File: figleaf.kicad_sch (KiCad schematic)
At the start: 70 parts, among them J1 Conn_01x02_Pin, J2 HRO_TYPE-C-31-M-14, J3 Battery, J9 TC2030_SWD, Q2 2N7002, SW1 PWR, SW2 RST, U1 SRV05-4, U10 MAX17048, U3 BQ24075, U8 nRF52840_moko_mk08

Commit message: data line thickness + mounting cuts
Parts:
- U8: footprint PCM_marbastlib-various:nRF52840_moko_mk08 -> Graz_Footprints:nRF52840_moko_mk08_GRAZ
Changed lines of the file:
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@@
 			)
 		)
-		(property "Footprint" "PCM_marbastlib-various:nRF52840_moko_mk08"
+		(property "Footprint" "Graz_Footprints:nRF52840_moko_mk08_GRAZ"
 			(at 87.63 118.11 90)
 			(effects

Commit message: testing m2 mounting holes
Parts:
- H1, H2, H3, H4, H5, H6, H7: footprint Graz_Footprints:m1.6 -> Graz_Footprints:MountingHole_M2_Graz
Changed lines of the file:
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@@
 			)
 		)
-		(property "Footprint" "Graz_Footprints:m1.6"
+		(property "Footprint" "Graz_Footprints:MountingHole_M2_Graz"
 			(at 43.18 176.53 0)
 			(effects
@@
 			)
 		)
-		(property "Footprint" "Graz_Footprints:m1.6"
+		(property "Footprint" "Graz_Footprints:MountingHole_M2_Graz"
 			(at 83.82 176.53 0)
 			(effects
@@
 			)
 		)
-		(property "Footprint" "Graz_Footprints:m1.6"
+		(property "Footprint" "Graz_Footprints:MountingHole_M2_Graz"
 			(at 63.5 176.53 0)
 			(effects
@@
 			)
 		)
-		(property "Footprint" "Graz_Footprints:m1.6"
+		(property "Footprint" "Graz_Footprints:MountingHole_M2_Graz"
 			(at 22.86 191.77 0)
 			(effects
@@
 			)
 		)
-		(property "Footprint" "Graz_Footprints:m1.6"
+		(property "Footprint" "Graz_Footprints:MountingHole_M2_Graz"
 			(at 63.5 191.77 0)
 			(effects
@@
 			)
 		)
-		(property "Footprint" "Graz_Footprints:m1.6"
+		(property "Footprint" "Graz_Footprints:MountingHole_M2_Graz"
 			(at 43.18 191.77 0)
 			(effects
@@
 			)
 		)
-		(property "Footprint" "Graz_Footprints:m1.6"
+		(property "Footprint" "Graz_Footprints:MountingHole_M2_Graz"
 			(at 22.86 176.53 0)
 			(effects

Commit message: finish m2 refactor
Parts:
- added H8, H9: MountingHole, Graz_Footprints:MountingHole_M2_Graz, symbol Mechanical:MountingHole
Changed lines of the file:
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@@
 	)
 	(symbol
+		(lib_id "Mechanical:MountingHole")
+		(at 83.82 191.77 0)
+		(unit 1)
+		(exclude_from_sim no)
+		(in_bom no)
+		(on_board yes)
+		(dnp no)
+		(fields_autoplaced yes)
+		(property "Reference" "H8"
+			(at 86.36 190.4999 0)
+			(effects
+				(font
+					(size 1.27 1.27)
+				)
+				(justify left)
+			)
+		)
+		(property "Value" "MountingHole"
+			(at 86.36 193.0399 0)
+			(effects
+				(font
+					(size 1.27 1.27)
+				)
+				(justify left)
+			)
+		)
+		(property "Footprint" "Graz_Footprints:MountingHole_M2_Graz"
+			(at 83.82 191.77 0)
+			(effects
+				(font
+					(size 1.27 1.27)
+				)
+				(hide yes)
+			)
+		)
+		(property "Datasheet" "~"
+			(at 83.82 191.77 0)
+			(effects
+				(font
+					(size 1.27 1.27)
+				)
+				(hide yes)
+			)
+		)
+		(property "Description" "Mounting Hole without connection"
+			(at 83.82 191.77 0)
+			(effects
+				(font
+					(size 1.27 1.27)
+				)
+				(hide yes)
+			)
+		)
+		(instances
+			(project "figleaf"
+				(path "/49b93484-acc8-4f70-93bc-7a6072a35fe8"
+					(reference "H8")
+					(unit 1)
+				)
+			)
+		)
+	)
+	(symbol
 		(lib_id "Device:Polyfuse_Small")
 		(at 64.77 29.21 90)
@@
 					(unit 1)
 				)
+			)
+		)
+	)
+	(symbol
+		(lib_id "Mechanical:MountingHole")
+		(at 104.14 191.77 0)
+		(unit 1)
+		(exclude_from_sim no)
+		(in_bom no)
+		(on_board yes)
+		(dnp no)
+		(fields_autoplaced yes)
+		(property "Reference" "H9"
+			(at 106.68 190.4999 0)
+			(effects
+				(font
+					(size 1.27 1.27)
+				)
+				(justify left)
+			)
+		)
+		(property "Value" "MountingHole"
+			(at 106.68 193.0399 0)
+			(effects
+				(font
+					(size 1.27 1.27)
+				)
+				(justify left)
+			)
+		)
+		(property "Footprint" "Graz_Footprints:MountingHole_M2_Graz"
+			(at 104.14 191.77 0)
+			(effects
+				(font
+					(size 1.27 1.27)
+				)
+				(hide yes)
+			)
+		)
+		(property "Datasheet" "~"
+			(at 104.14 191.77 0)
+			(effects
+				(font
+					(size 1.27 1.27)
+				)
+				(hide yes)
+			)
+		)
+		(property "Description" "Mounting Hole without connection"
+			(at 104.14 191.77 0)
+			(effects
+				(font
+					(size 1.27 1.27)
+				)
+				(hide yes)
+			)
+		)
+		(instances
+			(project "figleaf"
+				(path "/49b93484-acc8-4f70-93bc-7a6072a35fe8"
+					(reference "H9")
+					(unit 1)
+				)

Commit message: pre right side
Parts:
- added TP1, TP2: TestPoint_Probe, TestPoint:TestPoint_Pad_D1.0mm, symbol Connector:TestPoint_Probe
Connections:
- net USB-D+: now also TP2.1
- net USB-D-: now also TP1.1
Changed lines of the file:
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@@
 	)
 	(junction
+		(at 67.31 101.6)
+		(diameter 0)
+		(color 0 0 0 0)
+	)
+	(junction
 		(at 93.98 158.75)
 		(diameter 0)
@@
 	)
 	(junction
+		(at 67.31 104.14)
+		(diameter 0)
+		(color 0 0 0 0)
+	)
+	(junction
 		(at 49.53 29.21)
 		(diameter 0)
@@
 	(wire
 		(pts
+			(xy 67.31 104.14) (xy 69.85 104.14)
+		)
+		(stroke
+			(width 0)
+			(type default)
+		)
+	)
+	(wire
+		(pts
 			(xy 349.25 142.24) (xy 354.33 142.24)
 		)
@@
 	(wire
 		(pts
+			(xy 64.77 99.06) (xy 69.85 99.06)
+		)
+		(stroke
+			(width 0)
+			(type default)
+		)
+	)
+	(wire
+		(pts
 			(xy 49.53 29.21) (xy 55.88 29.21)
 		)
@@
 	(wire
 		(pts
+			(xy 67.31 101.6) (xy 69.85 101.6)
+		)
+		(stroke
+			(width 0)
+			(type default)
+		)
+	)
+	(wire
+		(pts
 			(xy 313.69 127) (xy 313.69 132.08)
 		)
@@
 	(wire
 		(pts
+			(xy 64.77 104.14) (xy 67.31 104.14)
+		)
+		(stroke
+			(width 0)
+			(type default)
+		)
+	)
+	(wire
+		(pts
 			(xy 262.89 152.4) (xy 262.89 157.48)
 		)
@@
 	(wire
 		(pts
+			(xy 64.77 101.6) (xy 67.31 101.6)
+		)
+		(stroke
+			(width 0)
+			(type default)
+		)
+	)
+	(wire
+		(pts
 			(xy 267.97 127) (xy 267.97 132.08)
 		)
@@
 	(global_label "USB-D+"
 		(shape bidirectional)
-		(at 69.85 101.6 180)
+		(at 64.77 101.6 180)
 		(fields_autoplaced yes)
 		(effects
@@
 		)
 		(property "Intersheetrefs" "${INTERSHEET_REFS}"
-			(at 59.2121 101.6794 0)
+			(at 54.1321 101.6794 0)
 			(effects
 				(font
@@
 	(global_label "USB-D-"
 		(shape bidirectional)
-		(at 69.85 104.14 180)
+		(at 64.77 104.14 180)
 		(fields_autoplaced yes)
 		(effects
@@
 		)
 		(property "Intersheetrefs" "${INTERSHEET_REFS}"
-			(at 59.2121 104.2194 0)
+			(at 54.1321 104.2194 0)
 			(effects
 				(font
@@
 	)
 	(symbol
+		(lib_id "Connector:TestPoint_Probe")
+		(at 67.31 101.6 90)
+		(unit 1)
+		(exclude_from_sim no)
+		(in_bom yes)
+		(on_board yes)
+		(dnp no)
+		(fields_autoplaced yes)
+		(property "Reference" "TP2"
+			(at 65.7225 93.98 90)
+			(effects
+				(font
+					(size 1.27 1.27)
+				)
+			)
+		)
+		(property "Value" "TestPoint_Probe"
+			(at 65.7225 96.52 90)
+			(effects
+				(font
+					(size 1.27 1.27)
+				)
+			)
+		)
+		(property "Footprint" "TestPoint:TestPoint_Pad_D1.0mm"
+			(at 67.31 96.52 0)
+			(effects
+				(font
+					(size 1.27 1.27)
+				)
+				(hide yes)
+			)
+		)
+		(property "Datasheet" "~"
+			(at 67.31 96.52 0)
+			(effects
+				(font
+					(size 1.27 1.27)
+				)
+				(hide yes)
+			)
+		)
+		(property "Description" "test point (alternative probe-style design)"
+			(at 67.31 101.6 0)
+			(effects
+				(font
+					(size 1.27 1.27)
+				)
+				(hide yes)
+			)
+		)
+		(pin "1"
+		)
+		(instances
+			(project "figleaf"
+				(path "/49b93484-acc8-4f70-93bc-7a6072a35fe8"
+					(reference "TP2")
+					(unit 1)
+				)
+			)
+		)
+	)
+	(symbol
 		(lib_id "power:GND")
 		(at 344.17 106.68 180)
@@
 	)
 	(symbol
+		(lib_id "Connector:TestPoint_Probe")
+		(at 67.31 104.14 180)
+		(unit 1)
+		(exclude_from_sim no)
+		(in_bom yes)
+		(on_board yes)
+		(dnp no)
+		(fields_autoplaced yes)
+		(property "Reference" "TP1"
+			(at 68.58 104.4574 0)
+			(effects
+				(font
+					(size 1.27 1.27)
+				)
+				(justify right)
+			)
+		)
+		(property "Value" "TestPoint_Probe"
+			(at 68.58 106.9974 0)
+			(effects
+				(font
+					(size 1.27 1.27)
+				)
+				(justify right)
+			)
+		)
+		(property "Footprint" "TestPoint:TestPoint_Pad_D1.0mm"
+			(at 62.23 104.14 0)
+			(effects
+				(font
+					(size 1.27 1.27)
+				)
+				(hide yes)
+			)
+		)
+		(property "Datasheet" "~"
+			(at 62.23 104.14 0)
+			(effects
+				(font
+					(size 1.27 1.27)
+				)
+				(hide yes)
+			)
+		)
+		(property "Description" "test point (alternative probe-style design)"
+			(at 67.31 104.14 0)
+			(effects
+				(font
+					(size 1.27 1.27)
+				)
+				(hide yes)
+			)
+		)
+		(pin "1"
+		)
+		(instances
+			(project ""
+				(path "/49b93484-acc8-4f70-93bc-7a6072a35fe8"
+					(reference "TP1")
+					(unit 1)
+				)
+			)
+		)
+	)
+	(symbol
 		(lib_id "0_graz_symbols:SW_OKM")
 		(at 288.29 116.84 0)
@@
 	(symbol
 		(lib_id "power:+5V")
-		(at 69.85 99.06 90)
+		(at 64.77 99.06 90)
 		(unit 1)
 		(exclude_from_sim no)
@@
 		(dnp no)
 		(property "Reference" "#PWR051"
-			(at 73.66 99.06 0)
+			(at 68.58 99.06 0)
 			(effects
 				(font
@@
 		)
 		(property "Value" "+5V"
-			(at 64.135 99.06 90)
+			(at 59.055 99.06 90)
 			(effects
 				(font
@@
 		)
 		(property "Footprint" ""
-			(at 69.85 99.06 0)
+			(at 64.77 99.06 0)
 			(effects
 				(font
@@
 		)
 		(property "Datasheet" ""
-			(at 69.85 99.06 0)
+			(at 64.77 99.06 0)
 			(effects
 				(font
@@
 		)
 		(property "Description" "Power symbol creates a global label with name \"+5V\""
-			(at 69.85 99.06 0)
+			(at 64.77 99.06 0)
 			(effects
 				(font

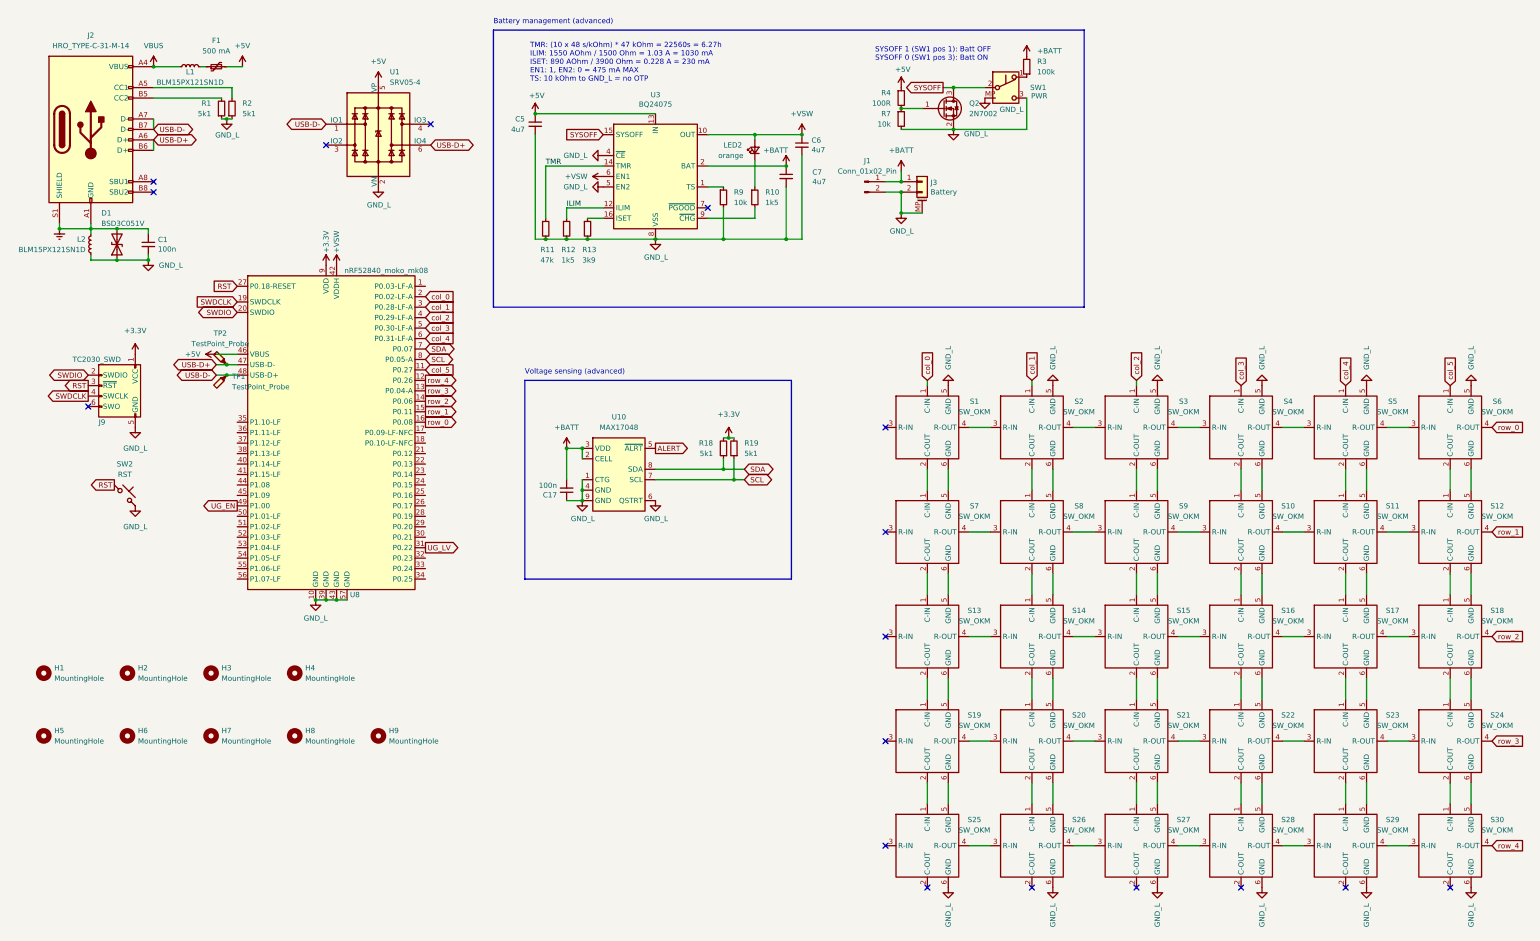
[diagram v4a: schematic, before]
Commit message: change GND_L to GND
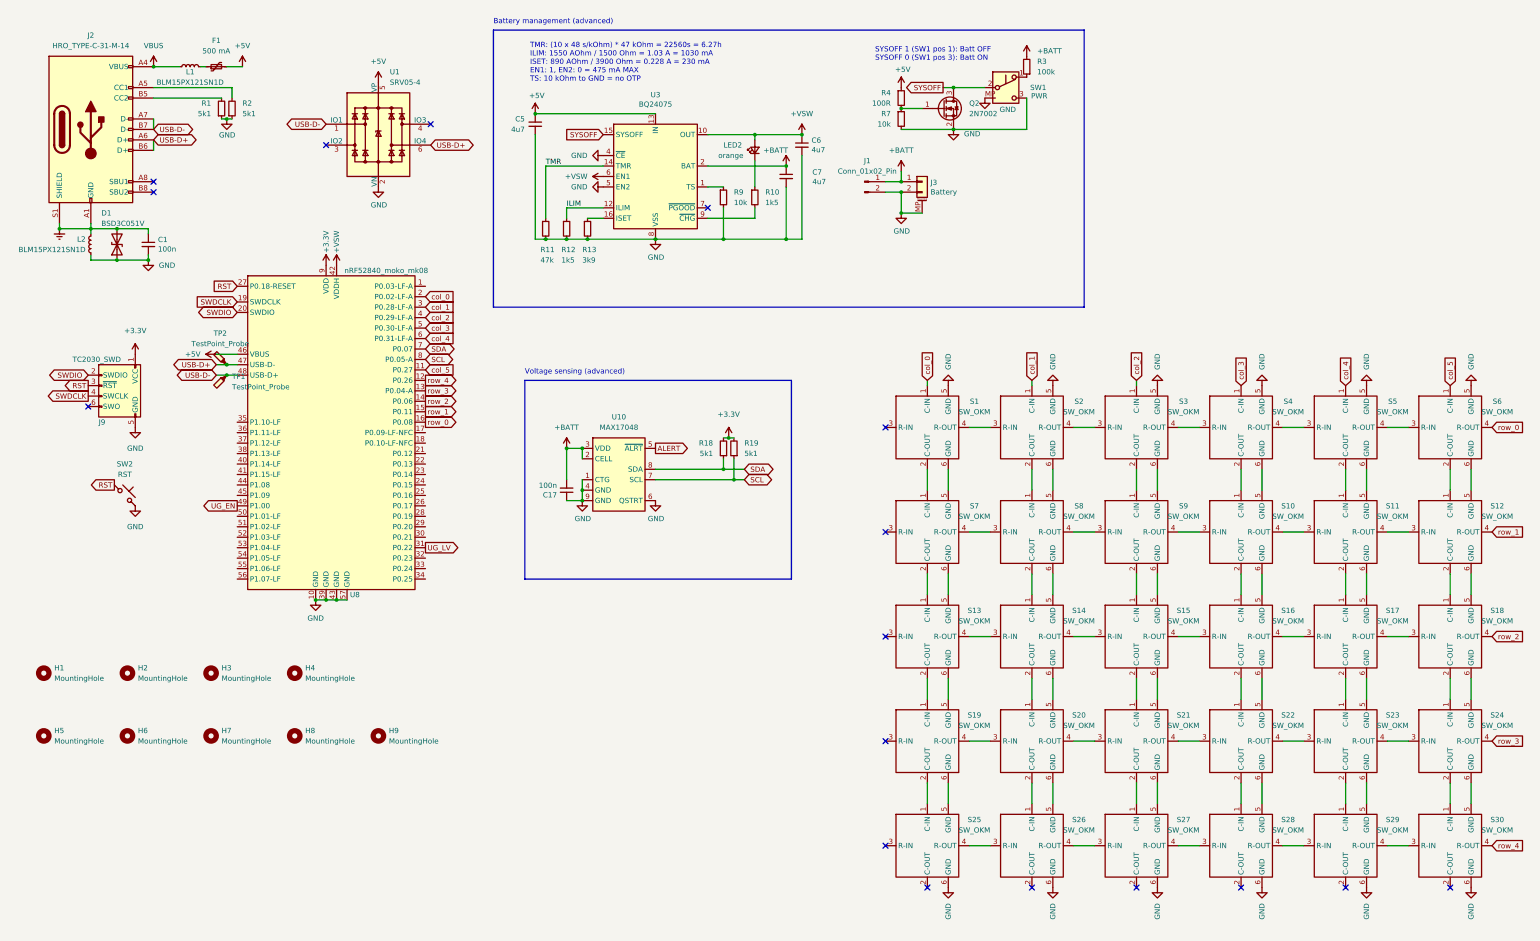
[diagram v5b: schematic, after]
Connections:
- net GND_L renamed GND
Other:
- note added: "TMR: (10 x 48 s/kOhm) * 47 kOhm = 22560s = 6.27h ILIM: 1550 AOhm / 1500 Ohm = 1.03 A = 1030 mA ISET: 890 AOhm / 3900 Ohm = 0.228 A = 230 mA EN1: 1, EN2: 0 = 475 mA MAX TS: 10 kOhm to GND = no OTP"
- note removed: "TMR: (10 x 48 s/kOhm) * 47 kOhm = 22560s = 6.27h ILIM: 1550 AOhm / 1500 Ohm = 1.03 A = 1030 mA ISET: 890 AOhm / 3900 Ohm = 0.228 A = 230 mA EN1: 1, EN2: 0 = 475 mA MAX TS: 10 kOhm to GND_L = no OTP"
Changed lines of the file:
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@@
 		)
 	)
-	(text "TMR: (10 x 48 s/kOhm) * 47 kOhm = 22560s = 6.27h\nILIM: 1550 AOhm / 1500 Ohm = 1.03 A = 1030 mA\nISET: 890 AOhm / 3900 Ohm = 0.228 A = 230 mA\nEN1: 1, EN2: 0 = 475 mA MAX\nTS: 10 kOhm to GND_L = no OTP"
+	(text "TMR: (10 x 48 s/kOhm) * 47 kOhm = 22560s = 6.27h\nILIM: 1550 AOhm / 1500 Ohm = 1.03 A = 1030 mA\nISET: 890 AOhm / 3900 Ohm = 0.228 A = 230 mA\nEN1: 1, EN2: 0 = 475 mA MAX\nTS: 10 kOhm to GND = no OTP"
 		(exclude_from_sim no)
 		(at 140.97 33.02 0)
@@
 			)
 		)
-		(property "Value" "GND_L"
+		(property "Value" "GND"
 			(at 154.94 50.7999 90)
 			(effects
@@
 			)
 		)
-		(property "Value" "GND_L"
+		(property "Value" "GND"
 			(at 369.5699 232.41 90)
 			(effects
@@
 			)
 		)
-		(property "Value" "GND_L"
+		(property "Value" "GND"
 			(at 255.016 39.624 0)
 			(effects
@@
 			)
 		)
-		(property "Value" "GND_L"
+		(property "Value" "GND"
 			(at 344.1701 102.87 90)
 			(effects
@@
 			)
 		)
-		(property "Value" "GND_L"
+		(property "Value" "GND"
 			(at 267.9701 102.87 90)
 			(effects
@@
 			)
 		)
-		(property "Value" "GND_L"
+		(property "Value" "GND"
 			(at 344.1699 232.41 90)
 			(effects
@@
 			)
 		)
-		(property "Value" "GND_L"
+		(property "Value" "GND"
 			(at 318.7699 232.41 90)
 			(effects
@@
 			)
 		)
-		(property "Value" "GND_L"
+		(property "Value" "GND"
 			(at 267.9699 232.41 90)
 			(effects
@@
 			)
 		)
-		(property "Value" "GND_L"
+		(property "Value" "GND"
 			(at 104.267 62.8142 0)
 			(effects
@@
 			)
 		)
-		(property "Value" "GND_L"
+		(property "Value" "GND"
 			(at 67.4116 45.8216 0)
 			(effects
@@
 			)
 		)
-		(property "Value" "GND_L"
+		(property "Value" "GND"
 			(at 45.085 121.92 0)
 			(effects
@@
 			)
 		)
-		(property "Value" "GND_L"
+		(property "Value" "GND"
 			(at 318.7701 102.87 90)
 			(effects
@@
 			)
 		)
-		(property "Value" "GND_L"
+		(property "Value" "GND"
 			(at 154.94 58.4199 90)
 			(effects
@@
 			)
 		)
-		(property "Value" "GND_L"
+		(property "Value" "GND"
 			(at 231.267 69.1642 0)
 			(effects
@@
 			)
 		)
-		(property "Value" "GND_L"
+		(property "Value" "GND"
 			(at 293.3699 232.41 90)
 			(effects
@@
 			)
 		)
-		(property "Value" "GND_L"
+		(property "Value" "GND"
 			(at 171.577 139.0142 0)
 			(effects
@@
 			)
 		)
-		(property "Value" "GND_L"
+		(property "Value" "GND"
 			(at 171.577 75.5142 0)
 			(effects
@@
 			)
 		)
-		(property "Value" "GND_L"
+		(property "Value" "GND"
 			(at 45.085 140.97 0)
 			(effects
@@
 			)
 		)
-		(property "Value" "GND_L"
+		(property "Value" "GND"
 			(at 50.8 77.4699 0)
 			(effects
@@
 			)
 		)
-		(property "Value" "GND_L"
+		(property "Value" "GND"
 			(at 153.797 139.0142 0)
 			(effects
@@
 			)
 		)
-		(property "Value" "GND_L"
+		(property "Value" "GND"
 			(at 242.5699 232.41 90)
 			(effects
@@
 			)
 		)
-		(property "Value" "GND_L"
+		(property "Value" "GND"
 			(at 246.38 45.5294 0)
 			(effects
@@
 			)
 		)
-		(property "Value" "GND_L"
+		(property "Value" "GND"
 			(at 293.3701 102.87 90)
 			(effects
@@
 			)
 		)
-		(property "Value" "GND_L"
+		(property "Value" "GND"
 			(at 242.5701 102.87 90)
 			(effects
@@
 			)
 		)
-		(property "Value" "GND_L"
+		(property "Value" "GND"
 			(at 369.5701 102.87 90)
 			(effects
@@
 			)
 		)
-		(property "Value" "GND_L"
+		(property "Value" "GND"
 			(at 88.9 163.195 0)
 			(effects

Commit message: v1 progress
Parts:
- removed C1, C17: 100n, Capacitor_SMD:C_0402_1005Metric, symbol Device:C_Small
- removed C5, C6, C7: 4u7, Capacitor_SMD:C_0402_1005Metric, symbol Device:C_Small
- removed D1: BSD3C051V, Diode_SMD:D_SOD-323, symbol Device:D_TVS
- removed F1: 500 mA, Fuse:Fuse_1206_3216Metric, symbol Device:Polyfuse_Small
- removed H1, H2, H3, H4, H5, H6, H7, H8, H9: MountingHole, Graz_Footprints:MountingHole_M2_Graz, symbol Mechanical:MountingHole
- removed J1: Conn_01x02_Pin, Graz_Footprints:Generic_Battery_Connector, symbol Connector:Conn_01x02_Pin
- removed J2: HRO_TYPE-C-31-M-14, PCM_marbastlib-various:USB_C_Receptacle_HRO_TYPE-C-31-M-14, symbol Connector:USB_C_Receptacle_USB2.0
- removed J3: Battery, Connector_JST:JST_SH_SM02B-SRSS-TB_1x02-1MP_P1.00mm_Horizontal, symbol Connector_Generic_MountingPin:Conn_01x02_MountingPin
- removed J9: TC2030_SWD, PCM_marbastlib-various:CON_TC2030_outlined, symbol PCM_marbastlib-various:TC2030_SWD
- removed L1, L2: BLM15PX121SN1D, Inductor_SMD:L_0402_1005Metric, symbol Device:L_Small
- removed LED2: orange, LED_SMD:LED_0402_1005Metric, symbol Device:LED_Small
- removed Q2: 2N7002, Package_TO_SOT_SMD:SOT-23, symbol Transistor_FET:2N7002
- removed R1, R18, R19, R2: 5k1, Resistor_SMD:R_0402_1005Metric, symbol Device:R_Small
- removed R10, R12: 1k5, Resistor_SMD:R_0402_1005Metric, symbol Device:R_Small
- removed R11: 47k, Resistor_SMD:R_0402_1005Metric, symbol Device:R_Small
- removed R13: 3k9, Resistor_SMD:R_0402_1005Metric, symbol Device:R_Small
- removed R3: 100k, Resistor_SMD:R_0402_1005Metric, symbol Device:R_Small
- removed R4: 100R, Resistor_SMD:R_0402_1005Metric, symbol Device:R_Small
- removed R7, R9: 10k, Resistor_SMD:R_0402_1005Metric, symbol Device:R_Small
- removed S1, S10, S11, S12, S13, S14, S15, S16, S17, S18, S19, S2, S20, S21, S22, S23, S24, S25, S26, S27, S28, S29, S3, S30, S4, S5, S6, S7, S8, S9: SW_OKM, Graz_Footprints:One Key Module Graz, symbol 0_graz_symbols:SW_OKM
- removed SW1: PWR, Graz_Footprints:SW_SSSS811101, symbol Switch:SW_Push_SPDT
- removed SW2: RST, Button_Switch_SMD:SW_SPST_B3U-3000P-B, symbol Switch:SW_Push_45deg
- removed TP1, TP2: TestPoint_Probe, TestPoint:TestPoint_Pad_D1.0mm, symbol Connector:TestPoint_Probe
- removed U1: SRV05-4, Package_TO_SOT_SMD:SOT-23-6, symbol Power_Protection:SRV05-4
- removed U10: MAX17048, Graz_Footprints:DFN-8-1EP_2x2mm_P0.5mm_EP0.7x1.3mm, symbol marbastlib-various:MAX17048
- removed U3: BQ24075, Package_DFN_QFN:VQFN-16-1EP_3x3mm_P0.5mm_EP1.6x1.6mm, symbol Battery_Management:BQ24075RGT
- removed U8: nRF52840_moko_mk08, Graz_Footprints:nRF52840_moko_mk08_GRAZ, symbol PCM_marbastlib-various:nRF52840_moko_mk08
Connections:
- no-connect marks 17 -> 0
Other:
- added sheet left (side.kicad_sch)
- added sheet right (side.kicad_sch)
- note removed: "Battery management (advanced)"
- note removed: "SYSOFF 1 (SW1 pos 1): Batt OFF SYSOFF 0 (SW1 pos 3): Batt ON"
- note removed: "TMR: (10 x 48 s/kOhm) * 47 kOhm = 22560s = 6.27h ILIM: 1550 AOhm / 1500 Ohm = 1.03 A = 1030 mA ISET: 890 AOhm / 3900 Ohm = 0.228 A = 230 mA EN1: 1, EN2: 0 = 475 mA MAX TS: 10 kOhm to GND = no OTP"
- note removed: "Voltage sensing (advanced)"
